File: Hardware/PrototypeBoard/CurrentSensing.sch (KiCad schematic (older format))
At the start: 6 parts, among them U5 TLI4970-D025T4, U6 TLI4970-D025T4, U7 TLI4970-D025T4

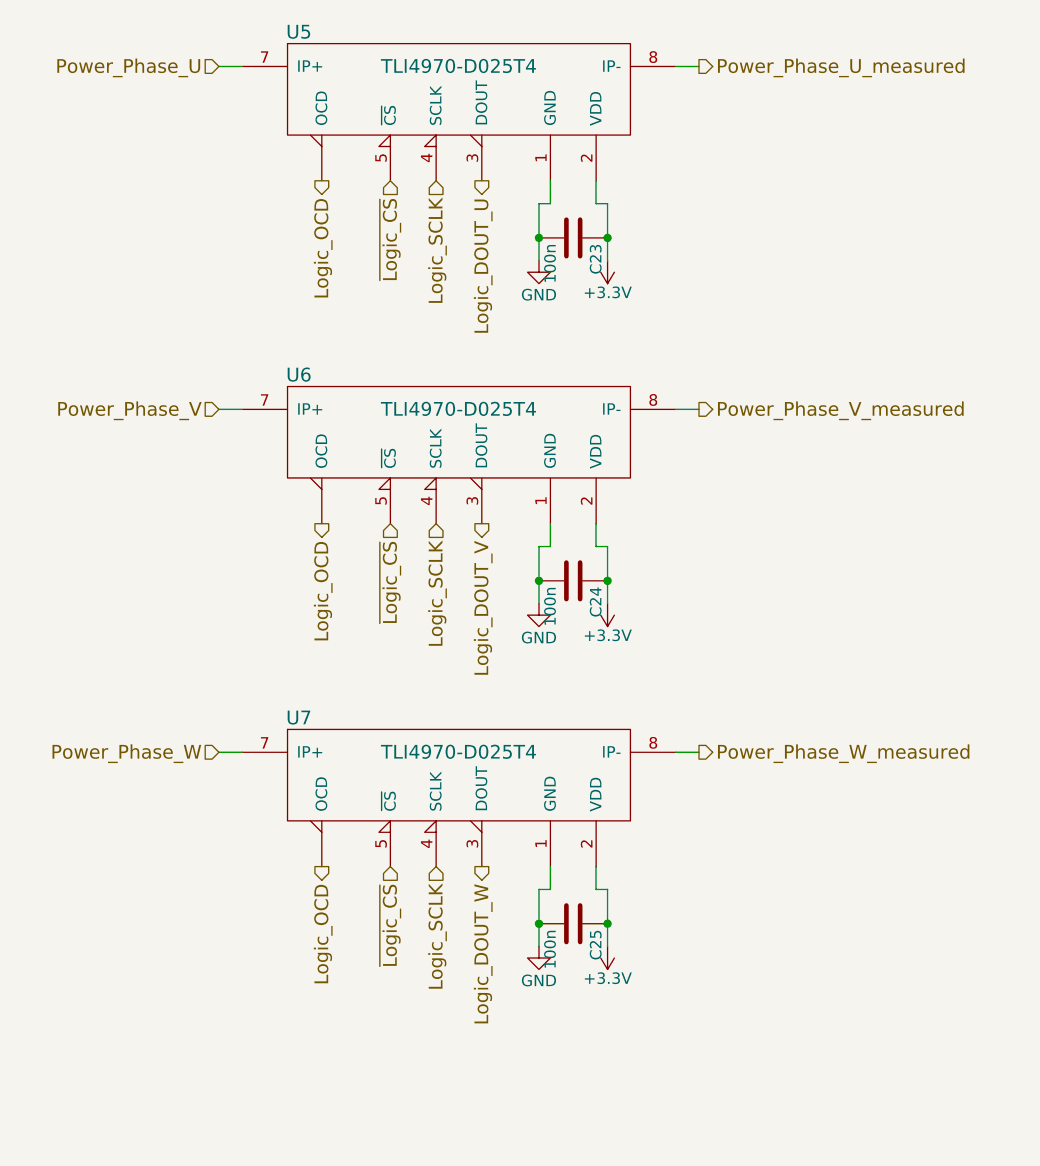
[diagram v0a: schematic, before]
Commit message: Fixed all ERC errors. Added power consumption estimation and other comments. Added links to datasheets. Dimensioned low pass and voltage dividers. Added TVS diodes for protection of voltage rails and ADC inputs. Added fuses. Added Testpoints. Added DC-link capacitors.
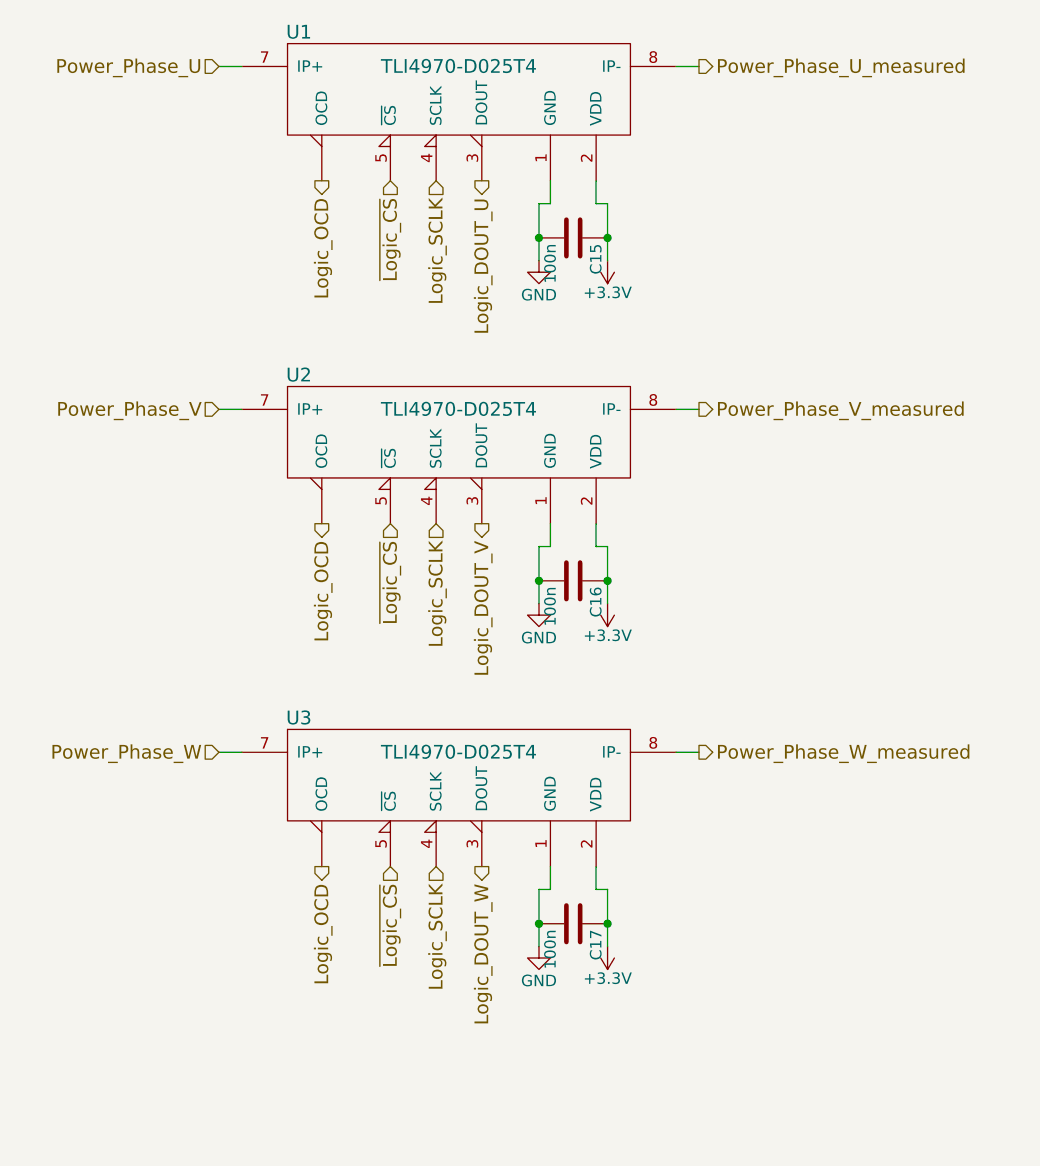
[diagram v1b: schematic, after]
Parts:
- renumbered C23 to C15, C24 to C16, C25 to C17, U5 to U1, U6 to U2, U7 to U3
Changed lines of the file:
@@
 $EndDescr
 $Comp
-L TLI4970-D025T4 U5
+L TLI4970-D025T4 U1
 U 1 1 56C11A3C
 P 4450 1200
-AR Path="/56D57CF9/56D58984/56C11A3C" Ref="U5"  Part="1"
-AR Path="/56D865C0/56D58984/56C11A3C" Ref="U9"  Part="1"
-F 0 "U5" H 3750 1350 60  0000 C CNN
+F 0 "U1" H 3750 1350 60  0000 C CNN
 F 1 "TLI4970-D025T4" H 4450 1200 60  0000 C CNN
 F 2 "" H 4450 1200 60  0001 C CNN
@@
 $EndComp
 $Comp
-L TLI4970-D025T4 U6
+L TLI4970-D025T4 U2
 U 1 1 56C11A9F
 P 4450 2700
-AR Path="/56D57CF9/56D58984/56C11A9F" Ref="U6"  Part="1"
-AR Path="/56D865C0/56D58984/56C11A9F" Ref="U10"  Part="1"
-F 0 "U6" H 3750 2850 60  0000 C CNN
+F 0 "U2" H 3750 2850 60  0000 C CNN
 F 1 "TLI4970-D025T4" H 4450 2700 60  0000 C CNN
 F 2 "" H 4450 2700 60  0001 C CNN
@@
 $EndComp
 $Comp
-L TLI4970-D025T4 U7
+L TLI4970-D025T4 U3
 U 1 1 56C11B3C
 P 4450 4200
-AR Path="/56D57CF9/56D58984/56C11B3C" Ref="U7"  Part="1"
-AR Path="/56D865C0/56D58984/56C11B3C" Ref="U11"  Part="1"
-F 0 "U7" H 3750 4350 60  0000 C CNN
+F 0 "U3" H 3750 4350 60  0000 C CNN
 F 1 "TLI4970-D025T4" H 4450 4200 60  0000 C CNN
 F 2 "" H 4450 4200 60  0001 C CNN
@@
 Power_Phase_V_measured
 $Comp
-L +3.3V #PWR054
+L +3.3V #PWR026
 U 1 1 56C11C4C
 P 5100 2050
-AR Path="/56D57CF9/56D58984/56C11C4C" Ref="#PWR054"  Part="1"
-AR Path="/56D865C0/56D58984/56C11C4C" Ref="#PWR079"  Part="1"
-F 0 "#PWR054" H 5100 1900 50  0001 C CNN
+F 0 "#PWR026" H 5100 1900 50  0001 C CNN
 F 1 "+3.3V" H 5100 2190 50  0000 C CNN
 F 2 "" H 5100 2050 50  0000 C CNN
@@
 $EndComp
 $Comp
-L GND #PWR055
+L GND #PWR027
 U 1 1 56C11D3E
 P 4800 2050
-AR Path="/56D57CF9/56D58984/56C11D3E" Ref="#PWR055"  Part="1"
-AR Path="/56D865C0/56D58984/56C11D3E" Ref="#PWR080"  Part="1"
-F 0 "#PWR055" H 4800 1800 50  0001 C CNN
+F 0 "#PWR027" H 4800 1800 50  0001 C CNN
 F 1 "GND" H 4800 1900 50  0000 C CNN
 F 2 "" H 4800 2050 50  0000 C CNN
@@
 $EndComp
 $Comp
-L C C23
+L C C15
 U 1 1 56C4BF7F
 P 4950 1950
-AR Path="/56D57CF9/56D58984/56C4BF7F" Ref="C23"  Part="1"
-AR Path="/56D865C0/56D58984/56C4BF7F" Ref="C32"  Part="1"
-F 0 "C23" H 4975 2050 50  0000 L CNN
+F 0 "C15" H 4975 2050 50  0000 L CNN
 F 1 "100n" H 4975 1850 50  0000 L CNN
 F 2 "Capacitors_SMD:C_0805_HandSoldering" H 4988 1800 50  0001 C CNN
@@
 Connection ~ 5100 1950
 $Comp
-L +3.3V #PWR056
+L +3.3V #PWR028
 U 1 1 56C4C285
 P 5100 3550
-AR Path="/56D57CF9/56D58984/56C4C285" Ref="#PWR056"  Part="1"
-AR Path="/56D865C0/56D58984/56C4C285" Ref="#PWR081"  Part="1"
-F 0 "#PWR056" H 5100 3400 50  0001 C CNN
+F 0 "#PWR028" H 5100 3400 50  0001 C CNN
 F 1 "+3.3V" H 5100 3690 50  0000 C CNN
 F 2 "" H 5100 3550 50  0000 C CNN
@@
 $EndComp
 $Comp
-L GND #PWR057
+L GND #PWR029
 U 1 1 56C4C28B
 P 4800 3550
-AR Path="/56D57CF9/56D58984/56C4C28B" Ref="#PWR057"  Part="1"
-AR Path="/56D865C0/56D58984/56C4C28B" Ref="#PWR082"  Part="1"
-F 0 "#PWR057" H 4800 3300 50  0001 C CNN
+F 0 "#PWR029" H 4800 3300 50  0001 C CNN
 F 1 "GND" H 4800 3400 50  0000 C CNN
 F 2 "" H 4800 3550 50  0000 C CNN
@@
 $EndComp
 $Comp
-L C C24
+L C C16
 U 1 1 56C4C291
 P 4950 3450
-AR Path="/56D57CF9/56D58984/56C4C291" Ref="C24"  Part="1"
-AR Path="/56D865C0/56D58984/56C4C291" Ref="C33"  Part="1"
-F 0 "C24" H 4975 3550 50  0000 L CNN
+F 0 "C16" H 4975 3550 50  0000 L CNN
 F 1 "100n" H 4975 3350 50  0000 L CNN
 F 2 "Capacitors_SMD:C_0805_HandSoldering" H 4988 3300 50  0001 C CNN
@@
 Connection ~ 5100 3450
 $Comp
-L +3.3V #PWR058
+L +3.3V #PWR030
 U 1 1 56C4C316
 P 5100 5050
-AR Path="/56D57CF9/56D58984/56C4C316" Ref="#PWR058"  Part="1"
-AR Path="/56D865C0/56D58984/56C4C316" Ref="#PWR083"  Part="1"
-F 0 "#PWR058" H 5100 4900 50  0001 C CNN
+F 0 "#PWR030" H 5100 4900 50  0001 C CNN
 F 1 "+3.3V" H 5100 5190 50  0000 C CNN
 F 2 "" H 5100 5050 50  0000 C CNN
@@
 $EndComp
 $Comp
-L GND #PWR059
+L GND #PWR031
 U 1 1 56C4C31C
 P 4800 5050
-AR Path="/56D57CF9/56D58984/56C4C31C" Ref="#PWR059"  Part="1"
-AR Path="/56D865C0/56D58984/56C4C31C" Ref="#PWR084"  Part="1"
-F 0 "#PWR059" H 4800 4800 50  0001 C CNN
+F 0 "#PWR031" H 4800 4800 50  0001 C CNN
 F 1 "GND" H 4800 4900 50  0000 C CNN
 F 2 "" H 4800 5050 50  0000 C CNN
@@
 $EndComp
 $Comp
-L C C25
+L C C17
 U 1 1 56C4C322
 P 4950 4950
-AR Path="/56D57CF9/56D58984/56C4C322" Ref="C25"  Part="1"
-AR Path="/56D865C0/56D58984/56C4C322" Ref="C34"  Part="1"
-F 0 "C25" H 4975 5050 50  0000 L CNN
+F 0 "C17" H 4975 5050 50  0000 L CNN
 F 1 "100n" H 4975 4850 50  0000 L CNN
 F 2 "Capacitors_SMD:C_0805_HandSoldering" H 4988 4800 50  0001 C CNN

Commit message: forgot files
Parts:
- U1, U2, U3: footprint (none) -> libs:PG-TISON-8-1
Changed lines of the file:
@@
 F 0 "U1" H 3750 1350 60  0000 C CNN
 F 1 "TLI4970-D025T4" H 4450 1200 60  0000 C CNN
-F 2 "" H 4450 1200 60  0001 C CNN
+F 2 "libs:PG-TISON-8-1" H 4450 1200 60  0001 C CNN
 F 3 "" H 4450 1200 60  0000 C CNN
 	1    4450 1200
@@
 F 0 "U2" H 3750 2850 60  0000 C CNN
 F 1 "TLI4970-D025T4" H 4450 2700 60  0000 C CNN
-F 2 "" H 4450 2700 60  0001 C CNN
+F 2 "libs:PG-TISON-8-1" H 4450 2700 60  0001 C CNN
 F 3 "" H 4450 2700 60  0000 C CNN
 	1    4450 2700
@@
 F 0 "U3" H 3750 4350 60  0000 C CNN
 F 1 "TLI4970-D025T4" H 4450 4200 60  0000 C CNN
-F 2 "" H 4450 4200 60  0001 C CNN
+F 2 "libs:PG-TISON-8-1" H 4450 4200 60  0001 C CNN
 F 3 "" H 4450 4200 60  0000 C CNN
 	1    4450 4200

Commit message: some more layout...
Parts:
- removed C17: 100n, Capacitors_SMD:C_0805_HandSoldering, symbol C
- added C15, C19: 100n, Capacitors_SMD:C_0805_HandSoldering, symbol C
- added C18, C20: 1μ, Capacitors_SMD:C_0805_HandSoldering, symbol C
- C16: value 100n -> 1μ
- renumbered C15 to C17
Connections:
- net +3V3: now also C15.1, C18.1, C19.1, C20.1
- net GND: now also C15.2, C18.2, C19.2, C20.2
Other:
- moved on the sheet: C17, U2, U3

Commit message: Migrated to kicad 5
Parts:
- C15, C16, C17, C18, C19, C20: symbol C -> Device:C
- U1, U2, U3: symbol TLI4970-D025T4 -> PrototypeBoard-rescue:TLI4970-D025T4
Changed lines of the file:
@@
-EESchema Schematic File Version 2
-LIBS:power
-LIBS:device
-LIBS:switches
-LIBS:relays
-LIBS:motors
-LIBS:transistors
-LIBS:conn
-LIBS:linear
-LIBS:regul
-LIBS:74xx
-LIBS:cmos4000
-LIBS:adc-dac
-LIBS:memory
-LIBS:xilinx
-LIBS:microcontrollers
-LIBS:dsp
-LIBS:microchip
-LIBS:analog_switches
-LIBS:motorola
-LIBS:texas
-LIBS:intel
-LIBS:audio
-LIBS:interface
-LIBS:digital-audio
-LIBS:philips
-LIBS:display
-LIBS:cypress
-LIBS:siliconi
-LIBS:opto
-LIBS:atmel
-LIBS:contrib
-LIBS:valves
+EESchema Schematic File Version 4
 LIBS:PrototypeBoard-cache
-EELAYER 25 0
+EELAYER 26 0
 EELAYER END
 $Descr A4 11693 8268
@@
 $EndDescr
 $Comp
-L TLI4970-D025T4 U1
+L PrototypeBoard-rescue:TLI4970-D025T4 U1
 U 1 1 56C11A3C
 P 4450 1200
@@
 $EndComp
 $Comp
-L TLI4970-D025T4 U2
+L PrototypeBoard-rescue:TLI4970-D025T4 U2
 U 1 1 56C11A9F
 P 4450 2900
@@
 $EndComp
 $Comp
-L TLI4970-D025T4 U3
+L PrototypeBoard-rescue:TLI4970-D025T4 U3
 U 1 1 56C11B3C
 P 4450 4600
@@
 Power_Phase_V_measured
 $Comp
-L +3.3V #PWR026
+L power:+3.3V #PWR026
 U 1 1 56C11C4C
 P 5100 4000
@@
 $EndComp
 $Comp
-L GND #PWR027
+L power:GND #PWR027
 U 1 1 56C11D3E
 P 4800 4000
@@
 	5400 4600 5500 4600
 $Comp
-L C C17
+L Device:C C17
 U 1 1 56C4BF7F
 P 4950 3600
@@
 $EndComp
 $Comp
-L C C18
+L Device:C C18
 U 1 1 5B20F200
 P 4950 3900
@@
 $EndComp
 $Comp
-L C C15
+L Device:C C15
 U 1 1 5B20F550
 P 4950 1900
@@
 $EndComp
 $Comp
-L C C19
+L Device:C C19
 U 1 1 5B20F5AE
 P 4950 5300
@@
 $EndComp
 $Comp
-L C C16
+L Device:C C16
 U 1 1 5B20F609
 P 4950 2200
@@
 $EndComp
 $Comp
-L C C20
+L Device:C C20
 U 1 1 5B20F677
 P 4950 5600
@@
 $EndComp
 $Comp
-L GND #PWR028
+L power:GND #PWR028
 U 1 1 5B20F6E2
 P 4800 2300
@@
 $EndComp
 $Comp
-L GND #PWR029
+L power:GND #PWR029
 U 1 1 5B20F708
 P 4800 5700
@@
 $EndComp
 $Comp
-L +3.3V #PWR030
+L power:+3.3V #PWR030
 U 1 1 5B20F72E
 P 5100 2300
@@
 $EndComp
 $Comp
-L +3.3V #PWR031
+L power:+3.3V #PWR031
 U 1 1 5B20F754
 P 5100 5700

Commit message: continued to work on new layout
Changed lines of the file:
@@
 $EndComp
 Wire Wire Line
-	5100 5200 5100 5700
+	5100 5200 5100 5300
 Connection ~ 5100 5600
 Connection ~ 5100 5300
 Wire Wire Line
-	4800 5200 4800 5700
+	4800 5200 4800 5300
 Connection ~ 4800 5300
 Connection ~ 4800 5600
 Wire Wire Line
-	4800 3500 4800 4000
+	4800 3500 4800 3600
 Wire Wire Line
-	5100 3500 5100 4000
+	5100 3500 5100 3600
 Connection ~ 5100 3600
 Connection ~ 4800 3600
@@
 Connection ~ 5100 3900
 Wire Wire Line
-	4800 1800 4800 2300
+	4800 1800 4800 1900
 Wire Wire Line
-	5100 1800 5100 2300
+	5100 1800 5100 1900
 Connection ~ 5100 1900
 Connection ~ 4800 1900
 Connection ~ 4800 2200
 Connection ~ 5100 2200
+Wire Wire Line
+	5100 5600 5100 5700
+Wire Wire Line
+	5100 5300 5100 5600
+Wire Wire Line
+	4800 5300 4800 5600
+Wire Wire Line
+	4800 5600 4800 5700
+Wire Wire Line
+	5100 3600 5100 3900
+Wire Wire Line
+	4800 3600 4800 3900
+Wire Wire Line
+	4800 3900 4800 4000
+Wire Wire Line
+	5100 3900 5100 4000
+Wire Wire Line
+	5100 1900 5100 2200
+Wire Wire Line
+	4800 1900 4800 2200
+Wire Wire Line
+	4800 2200 4800 2300
+Wire Wire Line
+	5100 2200 5100 2300
 $EndSCHEMATC
